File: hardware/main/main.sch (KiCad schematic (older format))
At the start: 68 parts, among them J1 Conn_01x06, J2 Conn_01x05, J3 Conn_01x01, J4 USB_B_Micro, J5 Conn_01x04, J7 Conn_01x02, J8 Conn_01x02, SW1 PEC12R-4217F-S0024, U1 E73-2G4M08S1C-52840, U10 DCX114YU, U12 NCV7428MW3, U2 MAX98357A, U3 MOC3043M, U4 SP3485, U5 NCV7428MW3, U6 BME680, U7 TPS82130, U8 D203S, U9 UG-2864ASWPG01, Y1 32768Hz

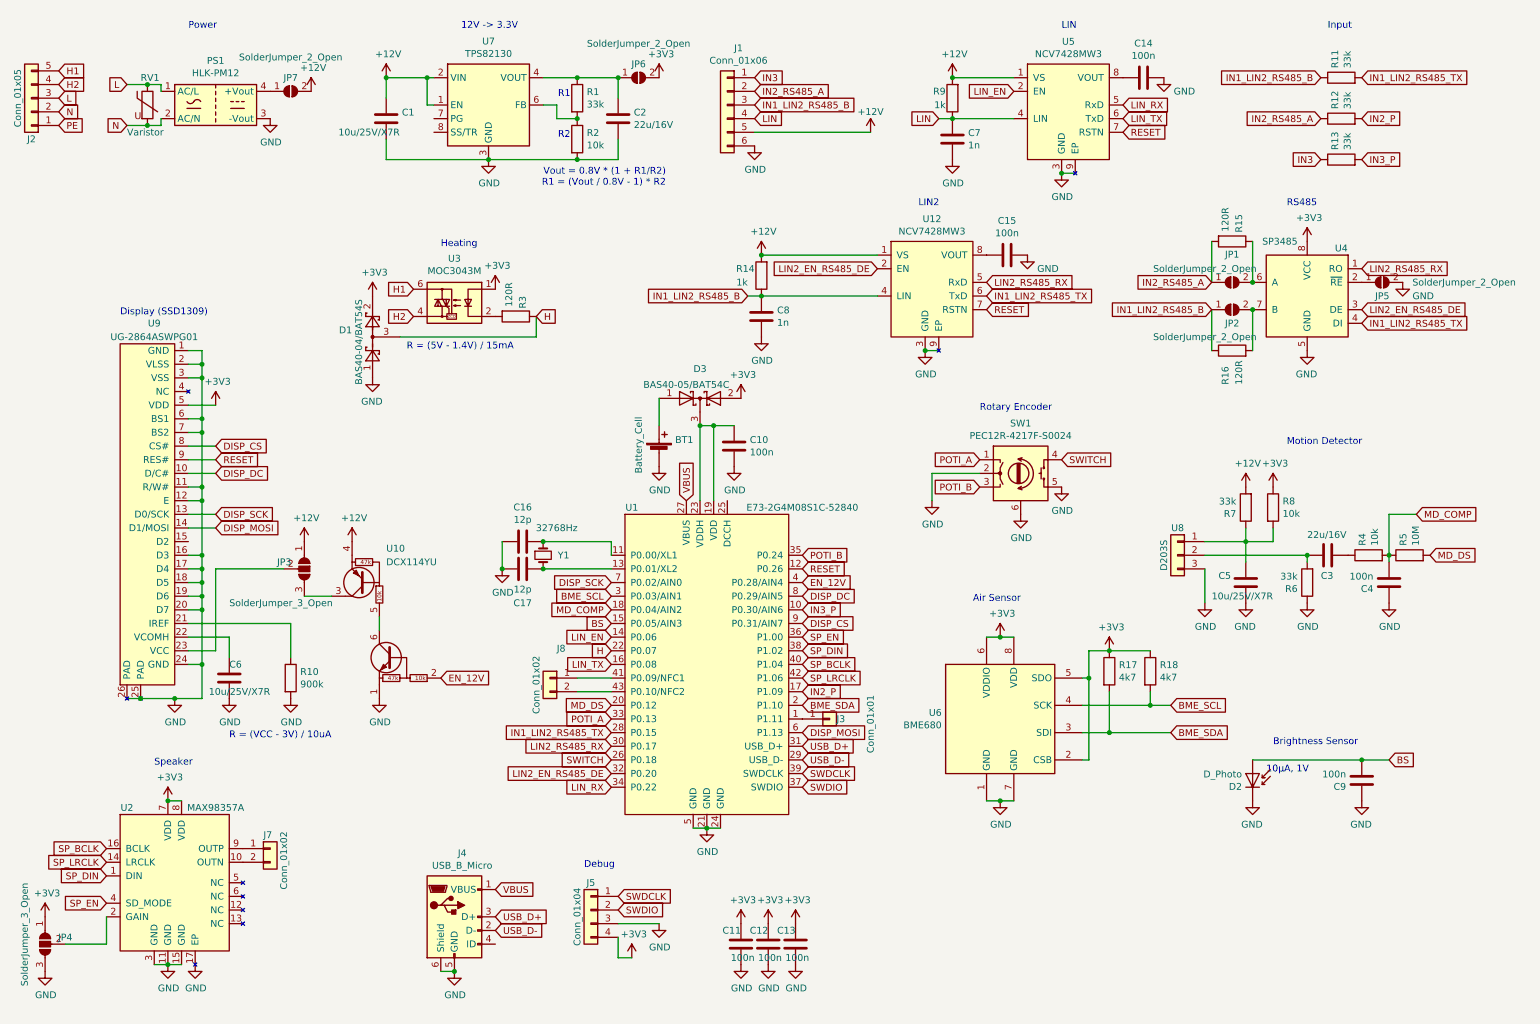
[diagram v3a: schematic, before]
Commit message: Add indicator LEDs to switch
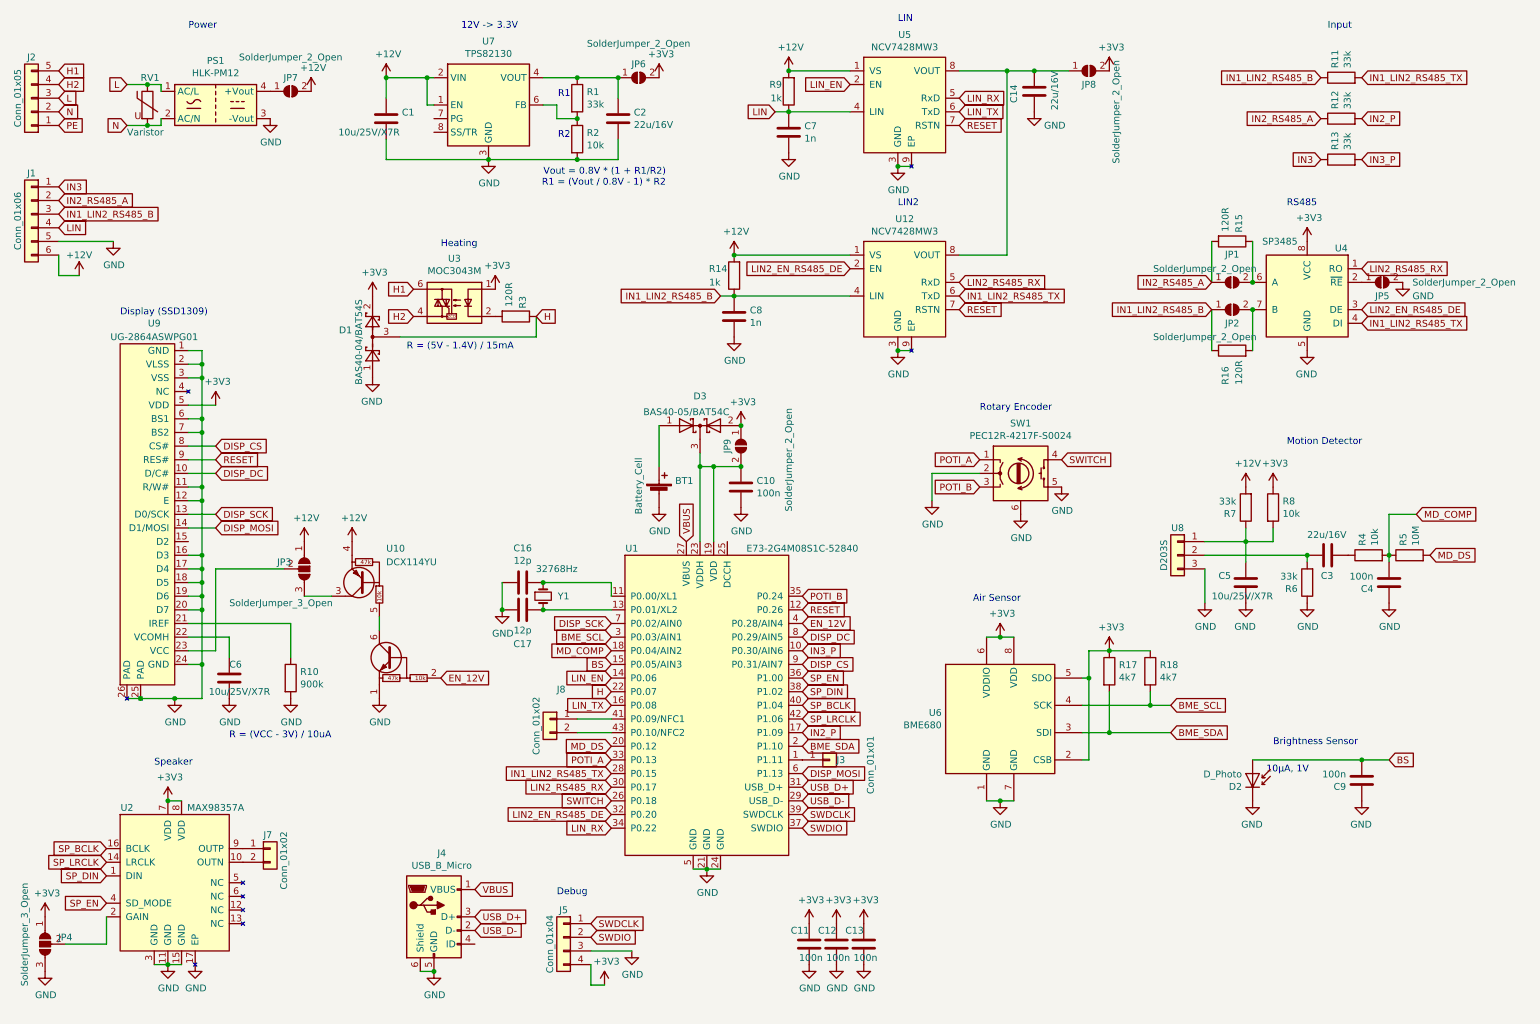
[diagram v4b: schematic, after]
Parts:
- removed C15: 100n, Capacitor_SMD:C_0603_1608Metric, symbol Device:C
- added JP8, JP9: SolderJumper_2_Open, RoomControl:Jumper2, symbol Jumper:SolderJumper_2_Open
- C14: value 100n -> 22u/16V; footprint Capacitor_SMD:C_0603_1608Metric -> Capacitor_SMD:C_0805_2012Metric
- D2: footprint Connector_PinHeader_2.54mm:PinHeader_1x02_P2.54mm_Vertical -> RoomControl:DiodeHoles
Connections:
- net +12V: now also J1.6 (Pin_6); no longer J1.5 (Pin_5)
- net +3V3: now also JP8.2 (B), JP9.1 (A)
- net GND: now also J1.5 (Pin_5); no longer J1.6 (Pin_6)
- net at C10.1, D3.3 (K), U1.19 (VDD)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: now also JP9.2 (B)
- net at C14.2, U5.8 (VOUT): now also U12.8 (VOUT), JP8.1 (A)
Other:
- moved on the sheet: BT1, C10, C11, C12, C13, C16, C17, C7, C8, D3, J1, J3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
